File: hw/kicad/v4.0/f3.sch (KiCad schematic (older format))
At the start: 34 parts, among them P11 USB_OTG, P12 CONN_01X04, P7 CONN_01X04, T1 testpoint, T2 testpoint, T44 testpoint, T45 testpoint, T46 testpoint, U21 USBLC6-4SC6, U25 STM32F303CBTx, U29 USBLC6-4SC6, Y1 8M

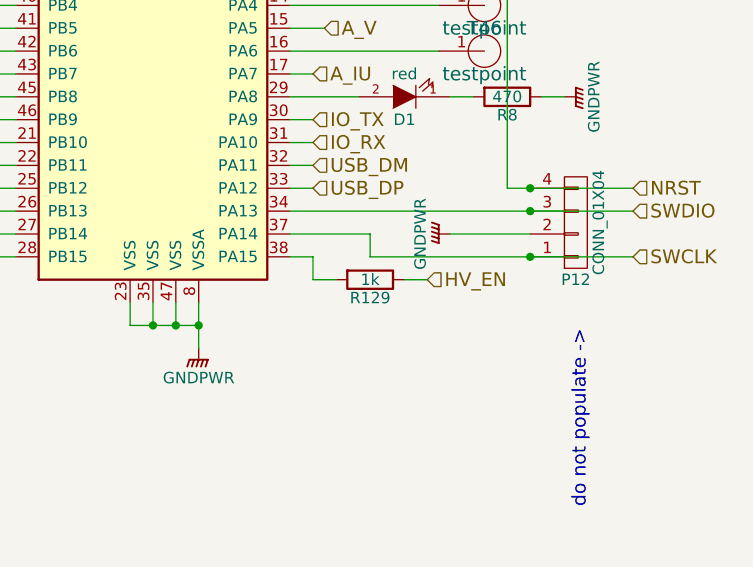
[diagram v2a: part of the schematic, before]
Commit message: changes for IKCM30F60GD
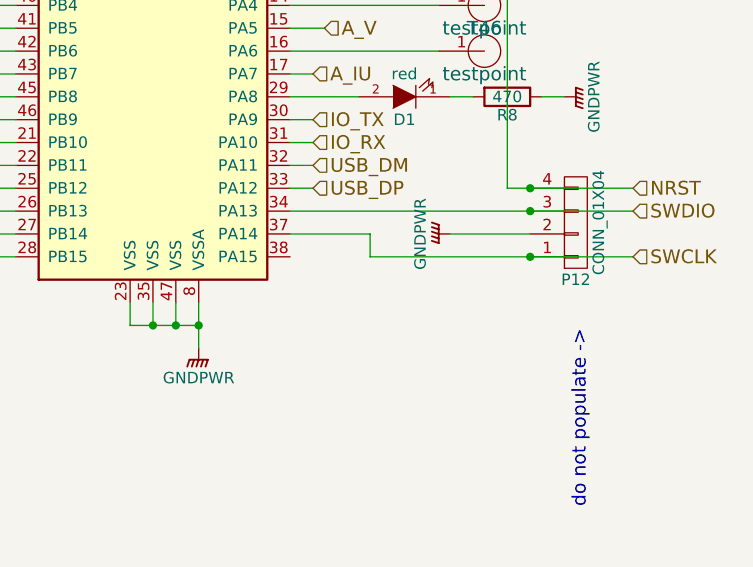
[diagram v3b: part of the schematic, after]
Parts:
- removed R129: 1k, stmbl:R_0603, symbol stmbl:R
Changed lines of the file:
@@
 	1    0    0    -1
-$EndComp
-$Comp
-L stmbl:R R129
-U 1 1 570E4A7D
-P 10750 4400
-F 0 "R129" V 10830 4400 50  0000 C CNN
-F 1 "1k" V 10750 4400 50  0000 C CNN
-F 2 "stmbl:R_0603" V 10680 4400 30  0001 C CNN
-F 3 "" H 10750 4400 30  0000 C CNN
-F 4 "" H 10750 4400 30  0001 C CNN "InternalName"
-F 5 "" H 10750 4400 30  0001 C CNN "Manufacturer No"
-F 6 "" H 10750 4400 30  0001 C CNN "Voltage"
-F 7 "" H 10750 4400 30  0001 C CNN "Source"
-F 8 "1%" H 10750 4400 30  0001 C CNN "Tolerance"
-F 9 "" H 0   0   50  0001 C CNN "Description"
-F 10 "" H 0   0   50  0001 C CNN "Manufacturer"
-	1    10750 4400
-	0    1    1    0
 $EndComp
 Text HLabel 10500 2900 2    60   Input ~ 0
@@
 Text HLabel 10500 3900 2    60   Input ~ 0
 USB_DM
-Text HLabel 11000 4400 2    60   Input ~ 0
-HV_EN
 Text HLabel 9100 3500 0    60   Input ~ 0
 HV_FLT
@@
 Wire Wire Line
 	10400 4000 10500 4000
-Wire Wire Line
-	10400 4300 10500 4300
-Wire Wire Line
-	11000 4400 10900 4400
-Wire Wire Line
-	10600 4400 10500 4400
-Wire Wire Line
-	10500 4400 10500 4300
 Connection ~ 11450 4300
 Connection ~ 11450 4100
